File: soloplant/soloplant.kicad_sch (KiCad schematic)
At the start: 9 parts, among them J1 282834-3, J2 282834-3, U1 PIC16F1829-I/P, U2 OPA2337PA

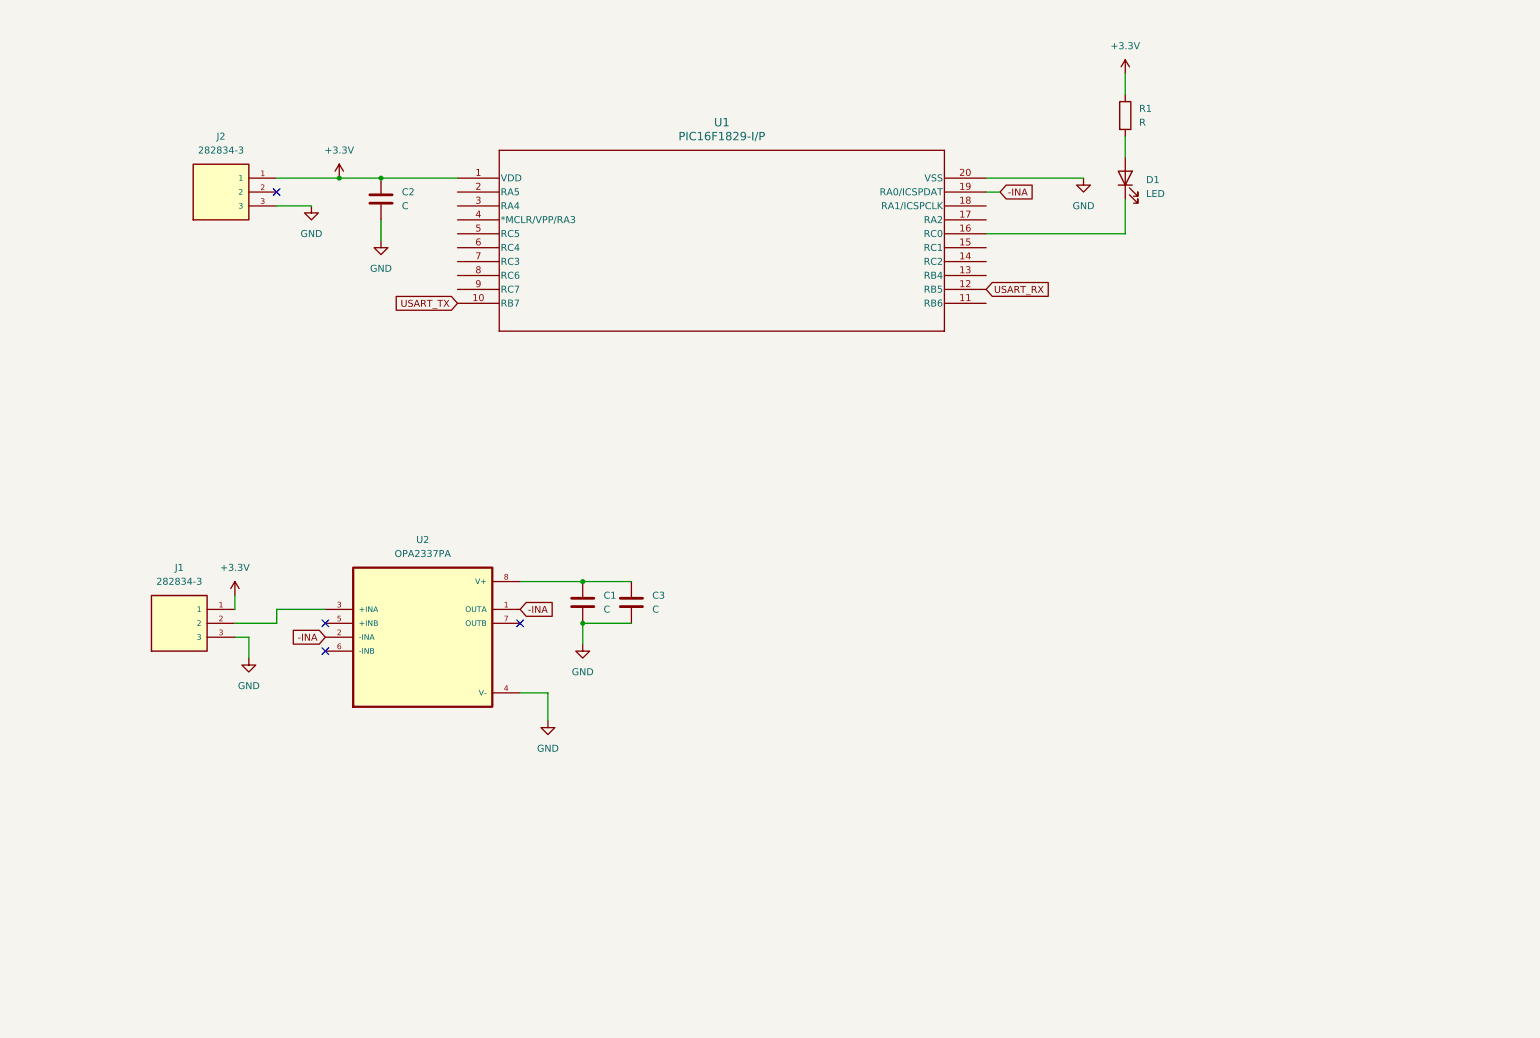
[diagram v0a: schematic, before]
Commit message: Added Term Block and Mosfet for Pump
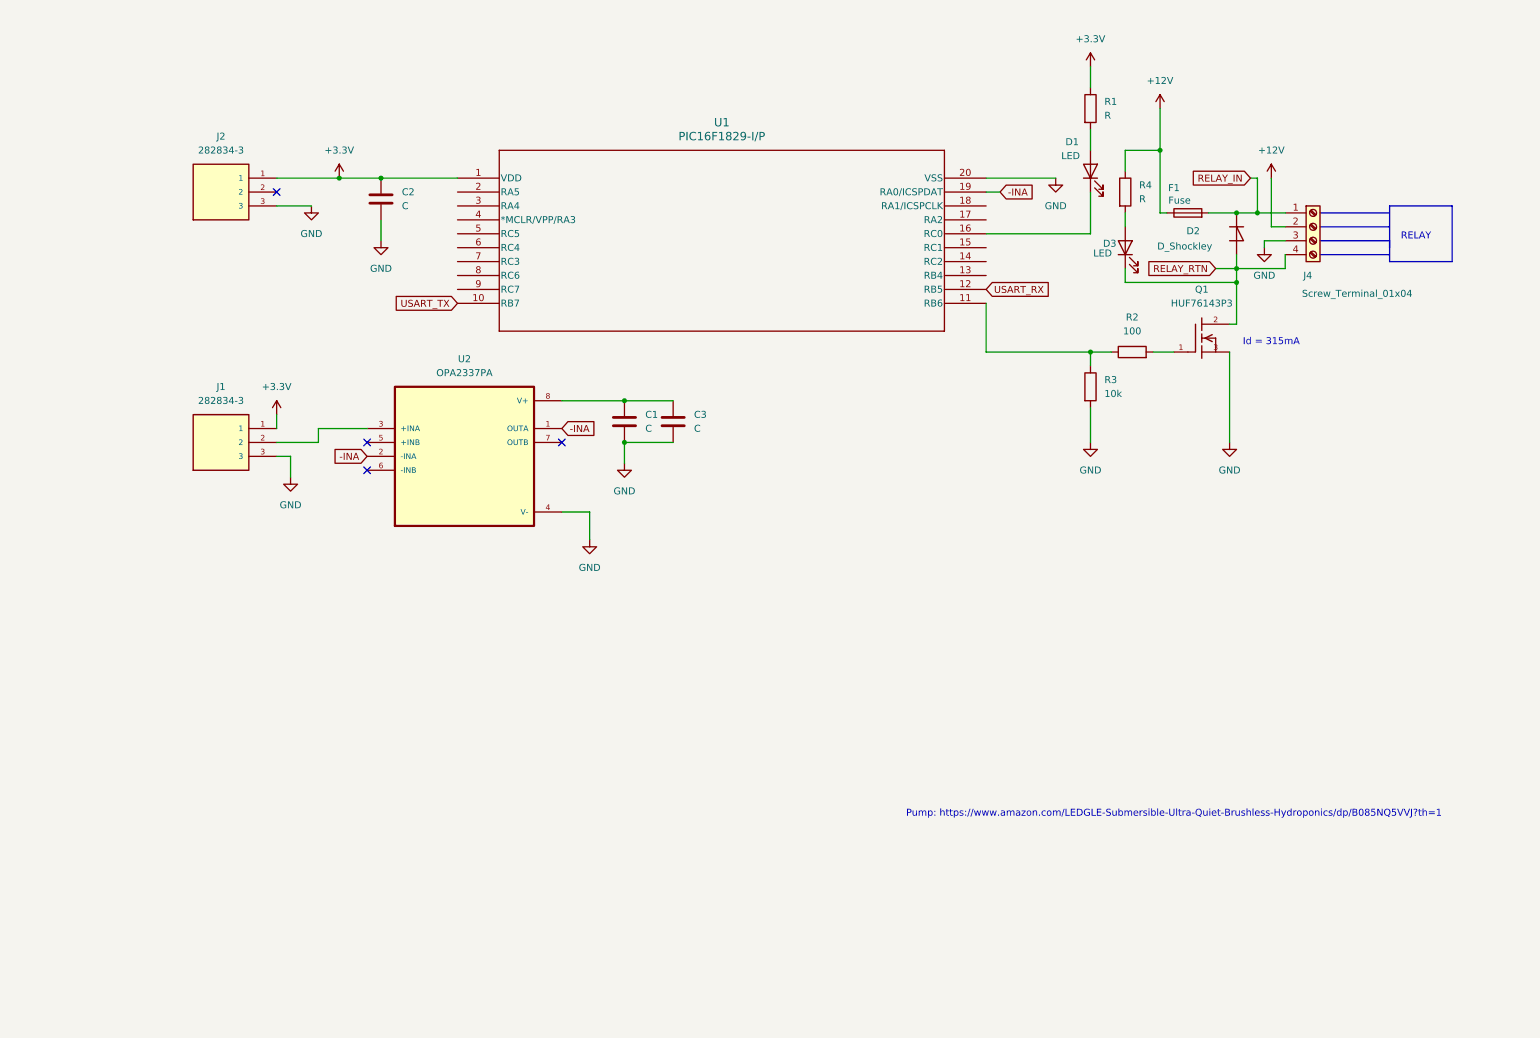
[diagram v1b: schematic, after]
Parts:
- added D2: D_Shockley, symbol Device:D_Shockley
- added D3: LED, symbol Device:LED
- added F1: Fuse, symbol Device:Fuse
- added J4: Screw_Terminal_01x04, symbol Connector:Screw_Terminal_01x04
- added Q1: HUF76143P3, HUF76143P3:HUF76143P3, symbol HUF76143P3:HUF76143P3
- added R2: 100, symbol Device:R
- added R3: 10k, symbol Device:R
- added R4: R, symbol Device:R
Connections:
- net GND: now also J4.3 (Pin_3), Q1.3, R3.2
- net at U1.11 (RB6): now also R2.1, R3.1
- new net: Q1.1, R2.2
- new net: D3.2 (A), R4.2
- new net +12V: F1.1, J4.2 (Pin_2), R4.1
- new net RELAY_IN: D2.1 (K), F1.2, J4.1 (Pin_1)
- new net RELAY_RTN: D2.2 (A), D3.1 (K), J4.4 (Pin_4), Q1.2
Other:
- note added: "Id = 315mA"
- note added: "Pump: https://www.amazon.com/LEDGLE-Submersible-Ultra-Quiet-Brushless-Hydroponics/dp/B085NQ5VVJ?th=1"
- note added: "RELAY"
- moved on the sheet: C1, C3, D1, J1, R1, U2

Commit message: Added New Parts and Expanded Circuit
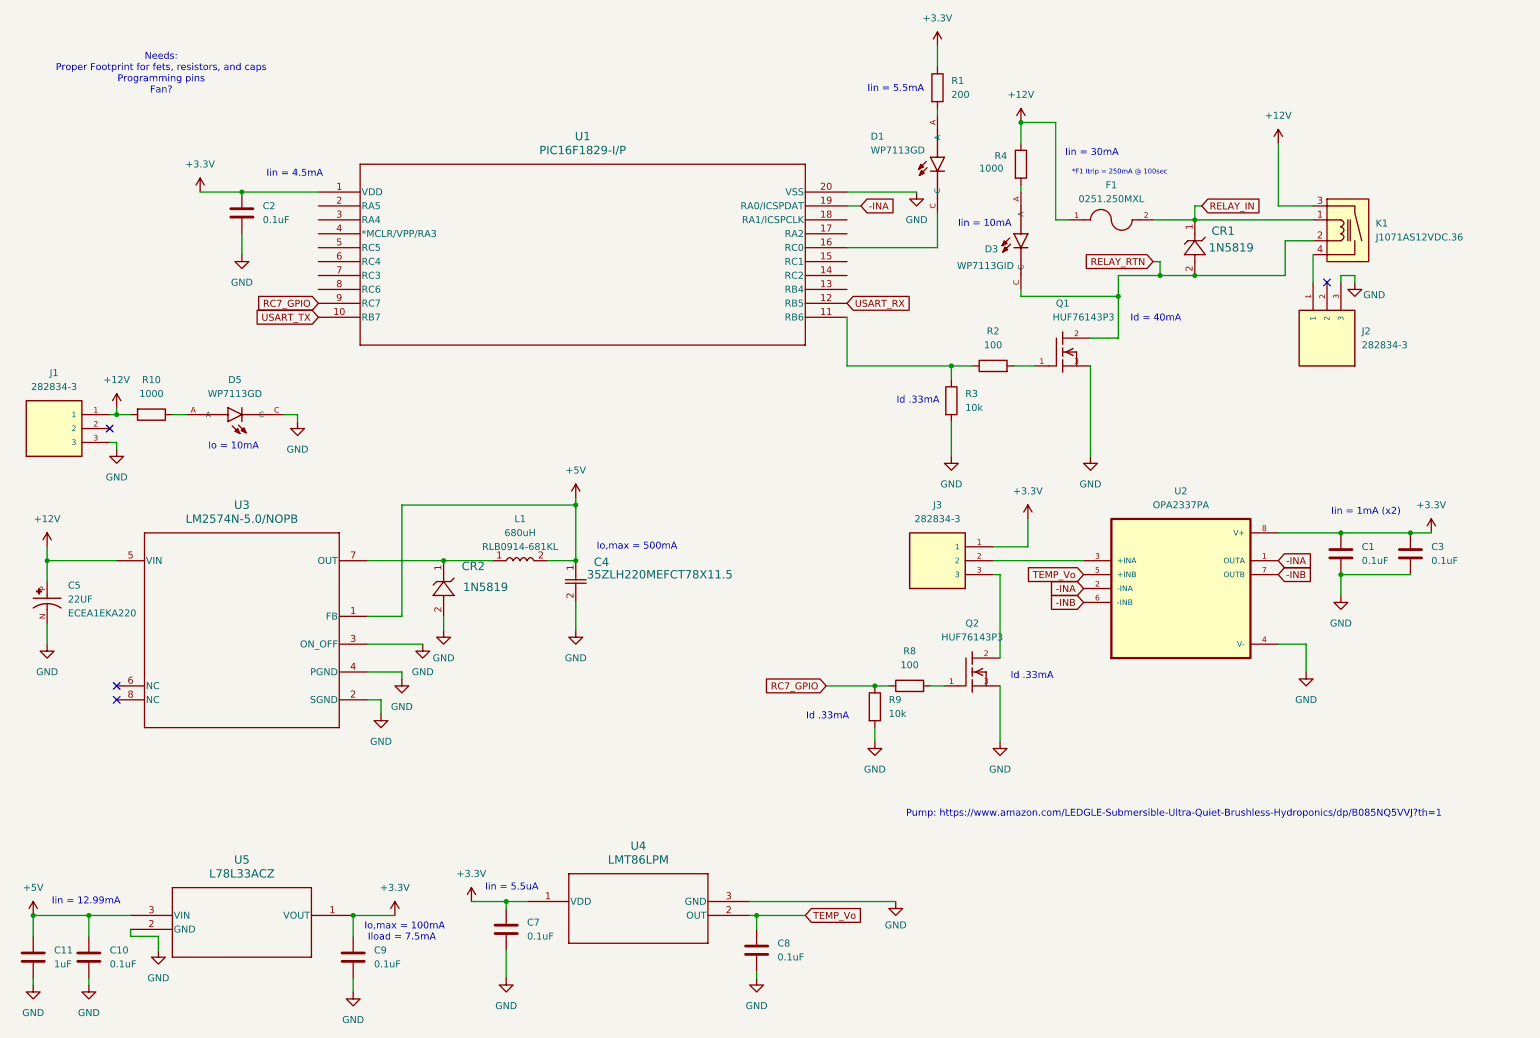
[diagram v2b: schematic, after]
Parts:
- removed D1, D3: LED, symbol Device:LED
- removed D2: D_Shockley, symbol Device:D_Shockley
- removed F1: Fuse, symbol Device:Fuse
- removed J4: Screw_Terminal_01x04, symbol Connector:Screw_Terminal_01x04
- added C10, C7, C8, C9: 0.1uF, symbol Device:C
- added C11: 1uF, symbol Device:C
- added C4: 35ZLH220MEFCT78X11.5, Local_Caps:35ZLH220MEFCT78X11_5, symbol Local_Caps:35ZLH220MEFCT78X11.5
- added C5: 22UF, Local_Caps:ECEA1EKA220, symbol Local_Caps:ECEA1EKA220
- added CR1, CR2: 1N5819, Local_Diodes:Shottky_1N5819, symbol Local_Diodes:1N5819
- added D1, D5: WP7113GD, LEDs:LED_WP7113GD, symbol LEDs:WP7113GD
- added D3: WP7113GID, LEDs:LED_WP7113GID, symbol LEDs:WP7113GID
- added F1: 0251.250MXL, Local_Fuses:FUSE_0251.250MXL, symbol Local_Fuses:0251.250MXL
- added J3: 282834-3, Local_Terminal_Block:TERM BLK 3P SIDE ENT 2_54MM, symbol TERM BLK 3P SIDE ENT 2_54MM:282834-3
- added K1: J1071AS12VDC.36, Local_Relay:RELAY_SPST_N.O._12VDC_30mA, symbol Relays:RELAY_SPST_N.O._12VDC_30mA
- added L1: 680uH, Local_Inductors:RLB0914-681KL, symbol Local_Inductor:RLB0914-681KL
- added Q2: HUF76143P3, HUF76143P3:HUF76143P3, symbol HUF76143P3:HUF76143P3
- added R10: 1000, symbol Device:R
- added R8: 100, symbol Device:R
- added R9: 10k, symbol Device:R
- added U3: LM2574N-5.0/NOPB, P0008A, symbol Local_Buck:LM2574N-5.0_NOPB
- added U4: LMT86LPM, Temp Sensor:LMT86LPM, symbol LMT86LPM:LMT86LPM
- added U5: L78L33ACZ, Local_V_Reg:L78L33ACZ, symbol Local_V_Reg:L78L33ACZ
- C1, C2, C3: value C -> 0.1uF
- J1, J2: footprint 282834-3:TE_282834-3 -> Local_Terminal_Block:TERM BLK 3P SIDE ENT 2_54MM
- R1: value R -> 200
- R4: value R -> 1000
- U1: footprint footprints:MCU_pic16f1829 -> Local_MCUs:MCU_pic16f1829
- U2: footprint OPA2337PA:DIP794W45P254L959H508Q8 -> Local_Op_Amps:DIP794W45P254L959H508Q8
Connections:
- net +12V: now also J1.1, C5.P, F1.1, K1.3, R10.2, U3.5 (VIN)
- net +3.3V: now also C1.1, C3.1, U2.8 (V+), C7.1, C9.1, J3.1, U4.1 (VDD), U5.1 (VOUT); no longer J1.1, J2.1
- net GND: now also C10.2, C11.2, C4.2, C5.N, C7.2, C8.2, C9.2, CR2.2, D5.C, Q2.3, R9.2, U3.2 (SGND), U3.3 (ON_OFF), U3.4 (PGND), U4.3 (GND), U5.2 (GND)
- net RELAY_IN: now also CR1.1, F1.2, K1.1
- net RELAY_RTN: now also CR1.2, D3.C, K1.2
- net at R1.2: now also D1.A
- net at U1.16 (RC0): now also D1.C
- net RC7_GPIO: now reaches U1.9 (RC7)
- net RC7_GPIO: now also R8.1, R9.1
- net at J1.2: no longer U2.3 (+INA)
- net TEMP_Vo: now reaches U2.5 (+INB)
- net TEMP_Vo: now also C8.1, U4.2 (OUT)
- net -INB: now reaches U2.6 (-INB)
- net -INB: now also U2.7 (OUTB)
- net at R4.2: now also D3.A
- new net: Q2.1, R8.2
- new net: J3.3, Q2.2
- new net: CR2.1, L1.1, U3.7 (OUT)
- new net: J2.1, K1.4
- new net: D5.A, R10.1
- new net: J3.2, U2.3 (+INA)
- new net +5V: C10.1, C11.1, C4.1, L1.2, U3.1 (FB), U5.3 (VIN)
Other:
- note added: "*F1 Itrip = 250mA @ 100sec"
- note added: "Id .33mA"
- note added: "Id = 40mA"
- note added: "Iin = 10mA"
- note added: "Iin = 12.99mA"
- note added: "Iin = 1mA (x2)"
- note added: "Iin = 30mA"
- note added: "Iin = 4.5mA"
- note added: "Iin = 5.5mA"
- note added: "Iin = 5.5uA"
- note added: "Iload = 7.5mA"
- note added: "Io = 10mA"
- note added: "Io,max = 100mA"
- note added: "Io,max = 500mA"
- note added: "Needs: Proper Footprint for fets, resistors, and caps Programming pins Fan?"
- note removed: "Id = 315mA"
- note removed: "RELAY"
- moved on the sheet: C1, C2, C3, Q1, R1, R2, R3, R4, U1, U2
